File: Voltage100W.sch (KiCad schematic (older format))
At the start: 2 parts

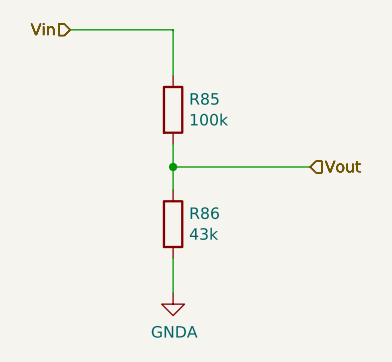
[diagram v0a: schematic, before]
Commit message: Petit ajustement pour accomoder le usb du arduino, pret pour routing
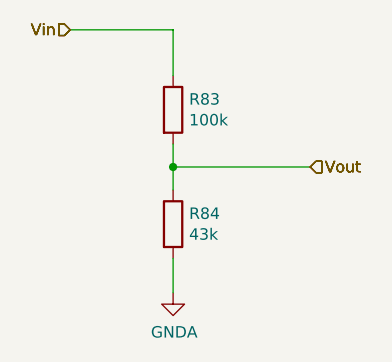
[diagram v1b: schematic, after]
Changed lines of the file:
@@
 $Descr A4 11693 8268
 encoding utf-8
-Sheet 47 80
+Sheet 45 80
 Title ""
 Date "2020-05-19"
@@
 AR Path="/5EF8B1F5/5EF90D23/5EFCF26A" Ref="R84"  Part="1"
 AR Path="/5EF8B1F5/5F05B51D/5EFCF26A" Ref="R86"  Part="1"
-F 0 "R86" H 4970 4646 50  0000 L CNN
+F 0 "R84" H 4970 4646 50  0000 L CNN
 F 1 "43k" H 4970 4555 50  0000 L CNN
 F 2 "Resistor_SMD:R_0805_2012Metric" V 4830 4600 50  0001 C CNN
@@
 AR Path="/5EF8B1F5/5EF90D23/5EE39ABF" Ref="R83"  Part="1"
 AR Path="/5EF8B1F5/5F05B51D/5EE39ABF" Ref="R85"  Part="1"
-F 0 "R85" H 4970 4146 50  0000 L CNN
+F 0 "R83" H 4970 4146 50  0000 L CNN
 F 1 "100k" H 4970 4055 50  0000 L CNN
 F 2 "Resistor_SMD:R_0805_2012Metric" V 4830 4100 50  0001 C CNN
@@
 AR Path="/5EF8B1F5/5EF90D23/6183CF98" Ref="#PWR0144"  Part="1"
 AR Path="/5EF8B1F5/5F05B51D/6183CF98" Ref="#PWR0150"  Part="1"
-F 0 "#PWR0150" H 4900 4650 50  0001 C CNN
+F 0 "#PWR0144" H 4900 4650 50  0001 C CNN
 F 1 "GNDA" H 4905 4727 50  0000 C CNN
 F 2 "" H 4900 4900 50  0001 C CNN

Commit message: retrait des test points inutiles
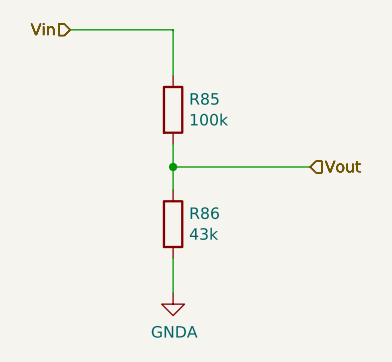
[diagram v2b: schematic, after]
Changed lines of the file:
@@
 AR Path="/5EF8B1F5/5EF90D23/5EFCF26A" Ref="R84"  Part="1"
 AR Path="/5EF8B1F5/5F05B51D/5EFCF26A" Ref="R86"  Part="1"
-F 0 "R84" H 4970 4646 50  0000 L CNN
+F 0 "R86" H 4970 4646 50  0000 L CNN
 F 1 "43k" H 4970 4555 50  0000 L CNN
 F 2 "Resistor_SMD:R_0805_2012Metric" V 4830 4600 50  0001 C CNN
@@
 AR Path="/5EF8B1F5/5EF90D23/5EE39ABF" Ref="R83"  Part="1"
 AR Path="/5EF8B1F5/5F05B51D/5EE39ABF" Ref="R85"  Part="1"
-F 0 "R83" H 4970 4146 50  0000 L CNN
+F 0 "R85" H 4970 4146 50  0000 L CNN
 F 1 "100k" H 4970 4055 50  0000 L CNN
 F 2 "Resistor_SMD:R_0805_2012Metric" V 4830 4100 50  0001 C CNN
@@
 AR Path="/5EF8B1F5/5EF90D23/6183CF98" Ref="#PWR0144"  Part="1"
 AR Path="/5EF8B1F5/5F05B51D/6183CF98" Ref="#PWR0150"  Part="1"
-F 0 "#PWR0144" H 4900 4650 50  0001 C CNN
+F 0 "#PWR0150" H 4900 4650 50  0001 C CNN
 F 1 "GNDA" H 4905 4727 50  0000 C CNN
 F 2 "" H 4900 4900 50  0001 C CNN

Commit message: Routed most of the power
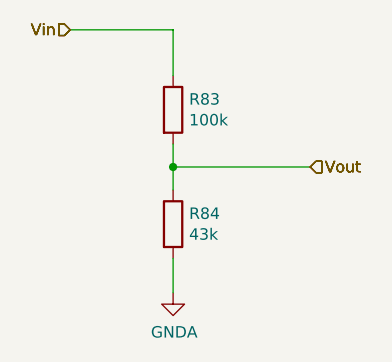
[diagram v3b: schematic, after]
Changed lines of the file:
@@
 AR Path="/5EF8B1F5/5EF90D23/5EFCF26A" Ref="R84"  Part="1"
 AR Path="/5EF8B1F5/5F05B51D/5EFCF26A" Ref="R86"  Part="1"
-F 0 "R86" H 4970 4646 50  0000 L CNN
+F 0 "R84" H 4970 4646 50  0000 L CNN
 F 1 "43k" H 4970 4555 50  0000 L CNN
 F 2 "Resistor_SMD:R_0805_2012Metric" V 4830 4600 50  0001 C CNN
@@
 AR Path="/5EF8B1F5/5EF90D23/5EE39ABF" Ref="R83"  Part="1"
 AR Path="/5EF8B1F5/5F05B51D/5EE39ABF" Ref="R85"  Part="1"
-F 0 "R85" H 4970 4146 50  0000 L CNN
+F 0 "R83" H 4970 4146 50  0000 L CNN
 F 1 "100k" H 4970 4055 50  0000 L CNN
 F 2 "Resistor_SMD:R_0805_2012Metric" V 4830 4100 50  0001 C CNN
@@
 AR Path="/5EF8B1F5/5EF90D23/6183CF98" Ref="#PWR0144"  Part="1"
 AR Path="/5EF8B1F5/5F05B51D/6183CF98" Ref="#PWR0150"  Part="1"
-F 0 "#PWR0150" H 4900 4650 50  0001 C CNN
+F 0 "#PWR0144" H 4900 4650 50  0001 C CNN
 F 1 "GNDA" H 4905 4727 50  0000 C CNN
 F 2 "" H 4900 4900 50  0001 C CNN
